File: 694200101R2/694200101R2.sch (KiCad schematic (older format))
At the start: 261 parts, among them J1 USB_C_Receptacle_USB2.0, J2 Conn_01x06_Male, J3 Conn_01x02_Male, SW1 MX_SW, SW10 MX_SW, SW100 MX_SW, SW101 MX_SW, SW102 MX_SW, SW103 MX_SW, SW104 MX_SW, SW105 MX_SW, SW106 MX_SW, SW107 MX_SW, SW11 MX_SW, SW12 MX_SW, SW13 MX_SW, SW14 MX_SW, SW15 MX_SW, SW16 MX_SW, SW17 MX_SW, SW18 MX_SW, SW19 MX_SW, SW2 MX_SW, SW20 MX_SW, SW21 MX_SW, SW22 MX_SW, SW23 MX_SW, SW24 MX_SW, SW25 MX_SW, SW26 MX_SW, SW27 MX_SW, SW28 MX_SW, SW29 MX_SW, SW3 MX_SW, SW30 MX_SW, SW31 MX_SW, SW32 MX_SW, SW33 MX_SW, SW34 MX_SW, SW35 MX_SW, SW36 MX_SW, SW37 MX_SW, SW38 MX_SW, SW39 MX_SW, SW4 MX_SW, SW40 MX_SW, SW41 MX_SW, SW42 MX_SW, SW43 MX_SW, SW44 MX_SW, SW45 MX_SW, SW46 MX_SW, SW47 MX_SW, SW48 MX_SW, SW49 MX_SW, SW5 MX_SW, SW50 MX_SW, SW51 MX_SW, SW52 MX_SW, SW53 MX_SW, SW54 MX_SW, SW55 MX_SW, SW56 MX_SW, SW57 MX_SW, SW58 MX_SW, SW59 MX_SW, SW6 MX_SW, SW60 MX_SW, SW61 MX_SW, SW62 MX_SW, SW63 MX_SW, SW64 MX_SW, SW65 MX_SW, SW66 MX_SW, SW67 MX_SW, SW68 MX_SW, SW69 MX_SW, SW7 MX_SW, SW70 MX_SW, SW71 MX_SW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

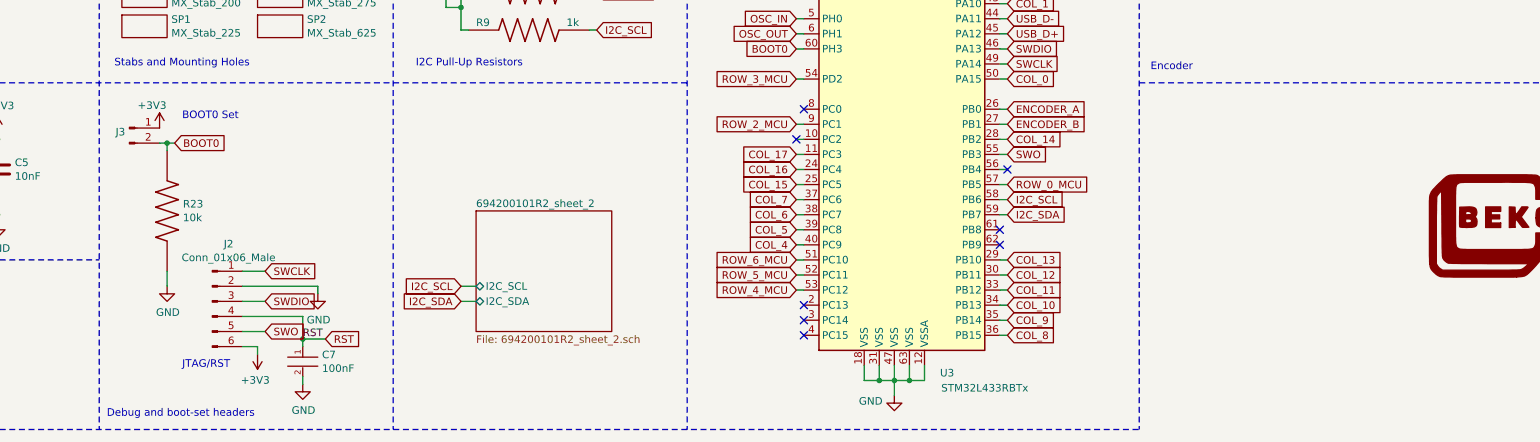
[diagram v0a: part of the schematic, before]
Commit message: Added BOOT0 Set and Reset Switches
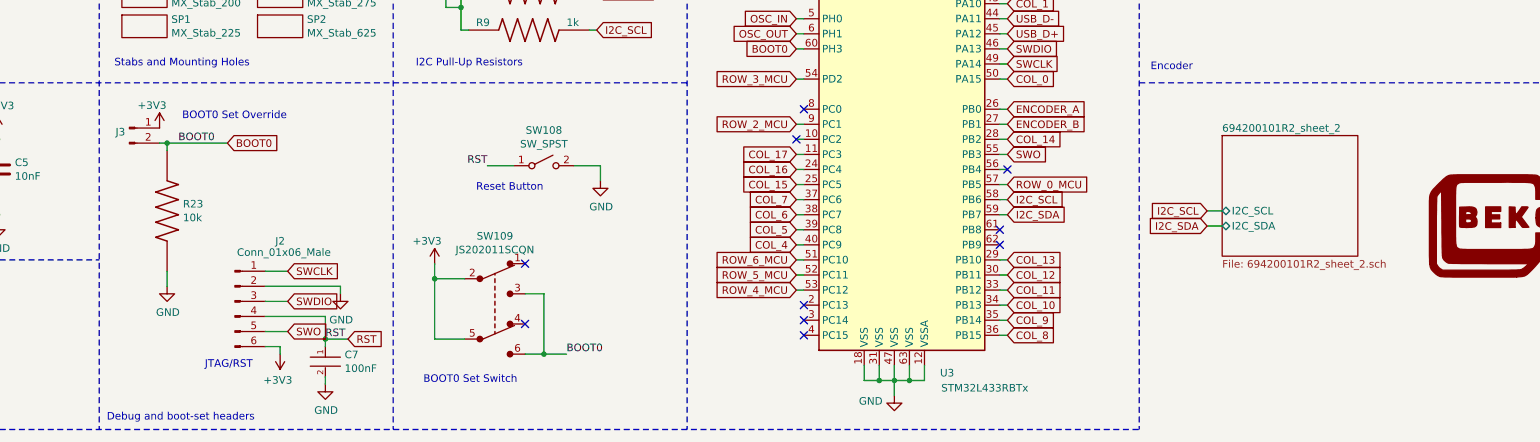
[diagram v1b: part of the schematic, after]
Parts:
- added SW108: SW_SPST, Button_Switch_SMD:SW_SPST_TL3342, symbol Switch:SW_SPST
- added SW109: JS202011SCQN, digikey-footprints:Switch_Slide_JS202011SCQN, symbol dk_Slide-Switches:JS202011SCQN
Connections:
- net +3V3: now also SW109.2, SW109.5
- net BOOT0: now also SW109.3, SW109.6
- net GND: now also SW108.2 (B)
- net RST: now also SW108.1 (A)
- no-connect marks 14 -> 16
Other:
- note added: "BOOT0 Set Override"
- note added: "BOOT0 Set Switch"
- note added: "Reset Button"
- note removed: "BOOT0 Set"
- moved on the sheet: C7, J2

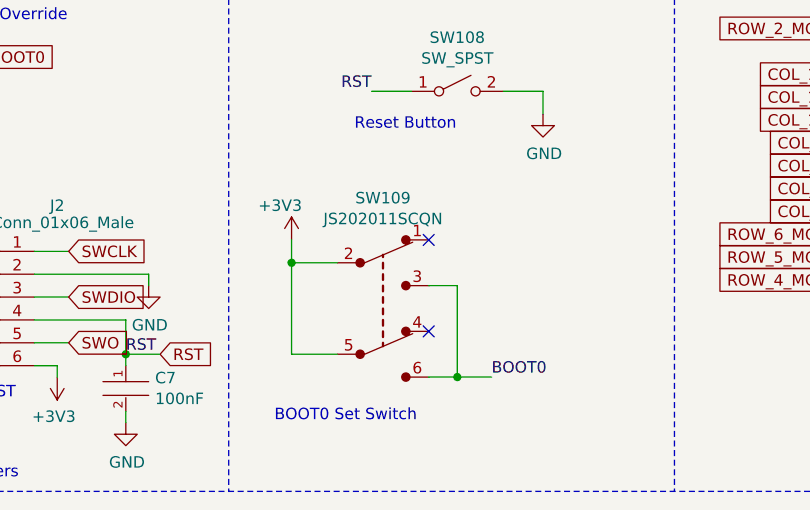
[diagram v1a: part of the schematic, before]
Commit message: Updated BOOT0 Switch to right angle switch
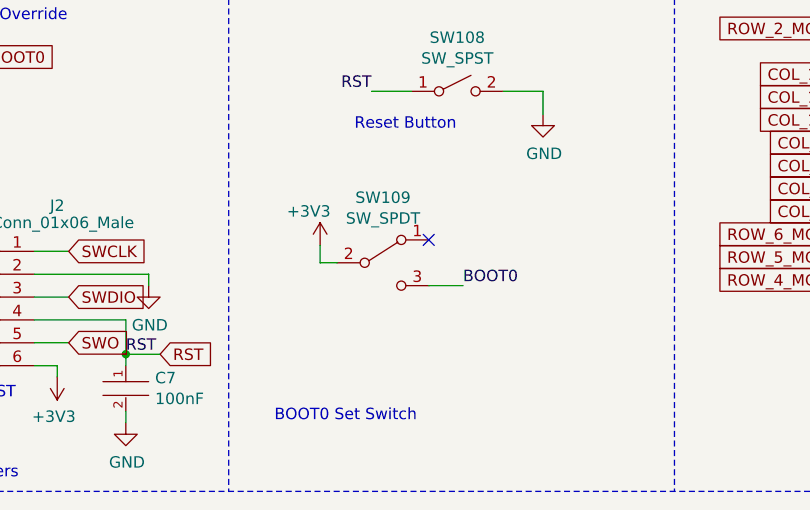
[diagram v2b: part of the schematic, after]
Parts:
- removed SW109: JS202011SCQN, digikey-footprints:Switch_Slide_JS202011SCQN, symbol dk_Slide-Switches:JS202011SCQN
- added SW109: SW_SPDT, Button_Switch_SMD:SW_SPDT_CK-JS102011SAQN, symbol Switch:SW_SPDT
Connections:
- net +3V3: now also SW109.2 (B)
- net BOOT0: now also SW109.3 (C)
- no-connect marks 16 -> 15
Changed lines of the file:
@@
 L power:+3V3 #PWR03
 U 1 1 630B8DFA
-P 6975 8600
-F 0 "#PWR03" H 6975 8450 50  0001 C CNN
-F 1 "+3V3" H 6925 8750 50  0000 C CNN
-F 2 "" H 6975 8600 50  0001 C CNN
-F 3 "" H 6975 8600 50  0001 C CNN
-	1    6975 8600
+P 7100 8625
+F 0 "#PWR03" H 7100 8475 50  0001 C CNN
+F 1 "+3V3" H 7050 8775 50  0000 C CNN
+F 2 "" H 7100 8625 50  0001 C CNN
+F 3 "" H 7100 8625 50  0001 C CNN
+	1    7100 8625
 	1    0    0    -1
 $EndComp
 Wire Wire Line
-	6975 8600 6975 8700
-Text Label 7850 9200 0    50   ~ 0
+	7100 8625 7100 8700
+Text Label 7725 8800 0    50   ~ 0
 BOOT0
-$Comp
-L dk_Slide-Switches:JS202011SCQN SW109
-U 1 1 63405795
-P 7375 8900
-F 0 "SW109" H 7375 9383 50  0000 C CNN
-F 1 "JS202011SCQN" H 7375 9292 50  0000 C CNN
-F 2 "digikey-footprints:Switch_Slide_JS202011SCQN" H 7575 9100 50  0001 L CNN
-F 3 "https://www.ckswitches.com/media/1422/js.pdf" H 7575 9200 60  0001 L CNN
-F 4 "401-2002-1-ND" H 7575 9300 60  0001 L CNN "Digi-Key_PN"
-F 5 "JS202011SCQN" H 7575 9400 60  0001 L CNN "MPN"
-F 6 "Switches" H 7575 9500 60  0001 L CNN "Category"
-F 7 "Slide Switches" H 7575 9600 60  0001 L CNN "Family"
-F 8 "https://www.ckswitches.com/media/1422/js.pdf" H 7575 9700 60  0001 L CNN "DK_Datasheet_Link"
-F 9 "/product-detail/en/c-k/JS202011SCQN/401-2002-1-ND/1640098" H 7575 9800 60  0001 L CNN "DK_Detail_Page"
-F 10 "SWITCH SLIDE DPDT 300MA 6V" H 7575 9900 60  0001 L CNN "Description"
-F 11 "C&K" H 7575 10000 60  0001 L CNN "Manufacturer"
-F 12 "Active" H 7575 10100 60  0001 L CNN "Status"
-	1    7375 8900
-	1    0    0    -1
-$EndComp
 Wire Wire Line
-	6975 8700 7175 8700
-Wire Wire Line
-	6975 8700 6975 9100
-Wire Wire Line
-	6975 9100 7175 9100
-Connection ~ 6975 8700
-NoConn ~ 7575 8600
-NoConn ~ 7575 9000
-Wire Wire Line
-	7575 8800 7700 8800
-Wire Wire Line
-	7700 8800 7700 9200
-Wire Wire Line
-	7700 9200 7575 9200
-Wire Wire Line
-	7700 9200 7850 9200
-Connection ~ 7700 9200
+	7100 8700 7175 8700
 Text Notes 6900 9400 0    50   ~ 0
 BOOT0 Set Switch
@@
 Text Notes 7250 8125 0    50   ~ 0
 Reset Button
+$Comp
+L Switch:SW_SPDT SW109
+U 1 1 62B1A803
+P 7375 8700
+F 0 "SW109" H 7375 8985 50  0000 C CNN
+F 1 "SW_SPDT" H 7375 8894 50  0000 C CNN
+F 2 "Button_Switch_SMD:SW_SPDT_CK-JS102011SAQN" H 7375 8700 50  0001 C CNN
+F 3 "~" H 7375 8700 50  0001 C CNN
+	1    7375 8700
+	1    0    0    -1
+$EndComp
+NoConn ~ 7575 8600
+Wire Wire Line
+	7575 8800 7725 8800
 $EndSCHEMATC

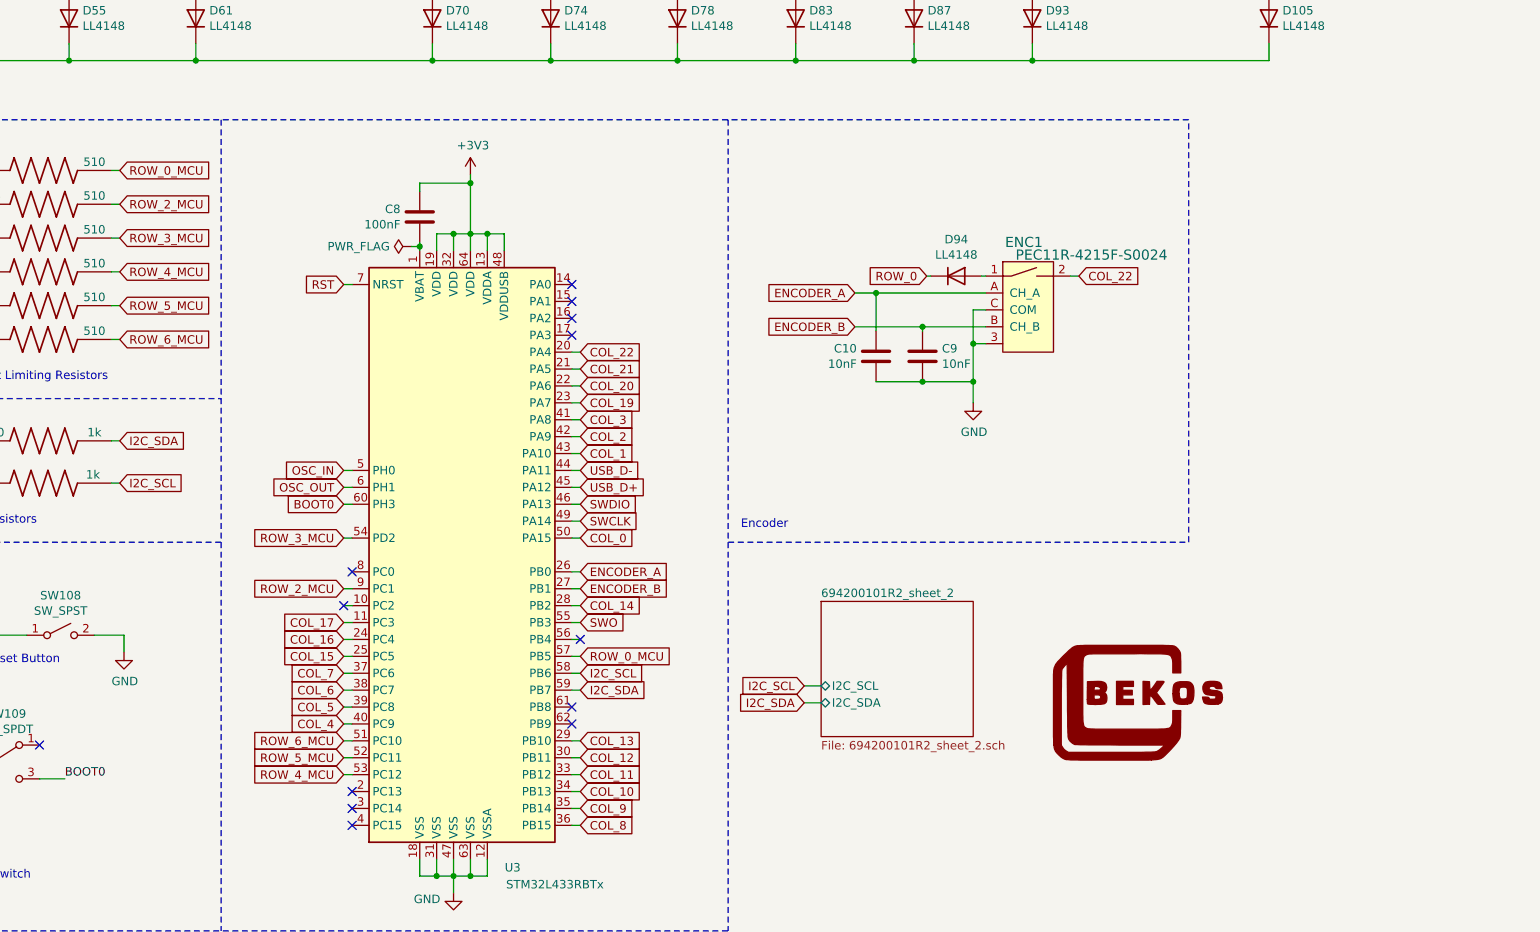
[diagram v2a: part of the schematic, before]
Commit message: Updated Schematic to use KiCad LED Driver Symbols
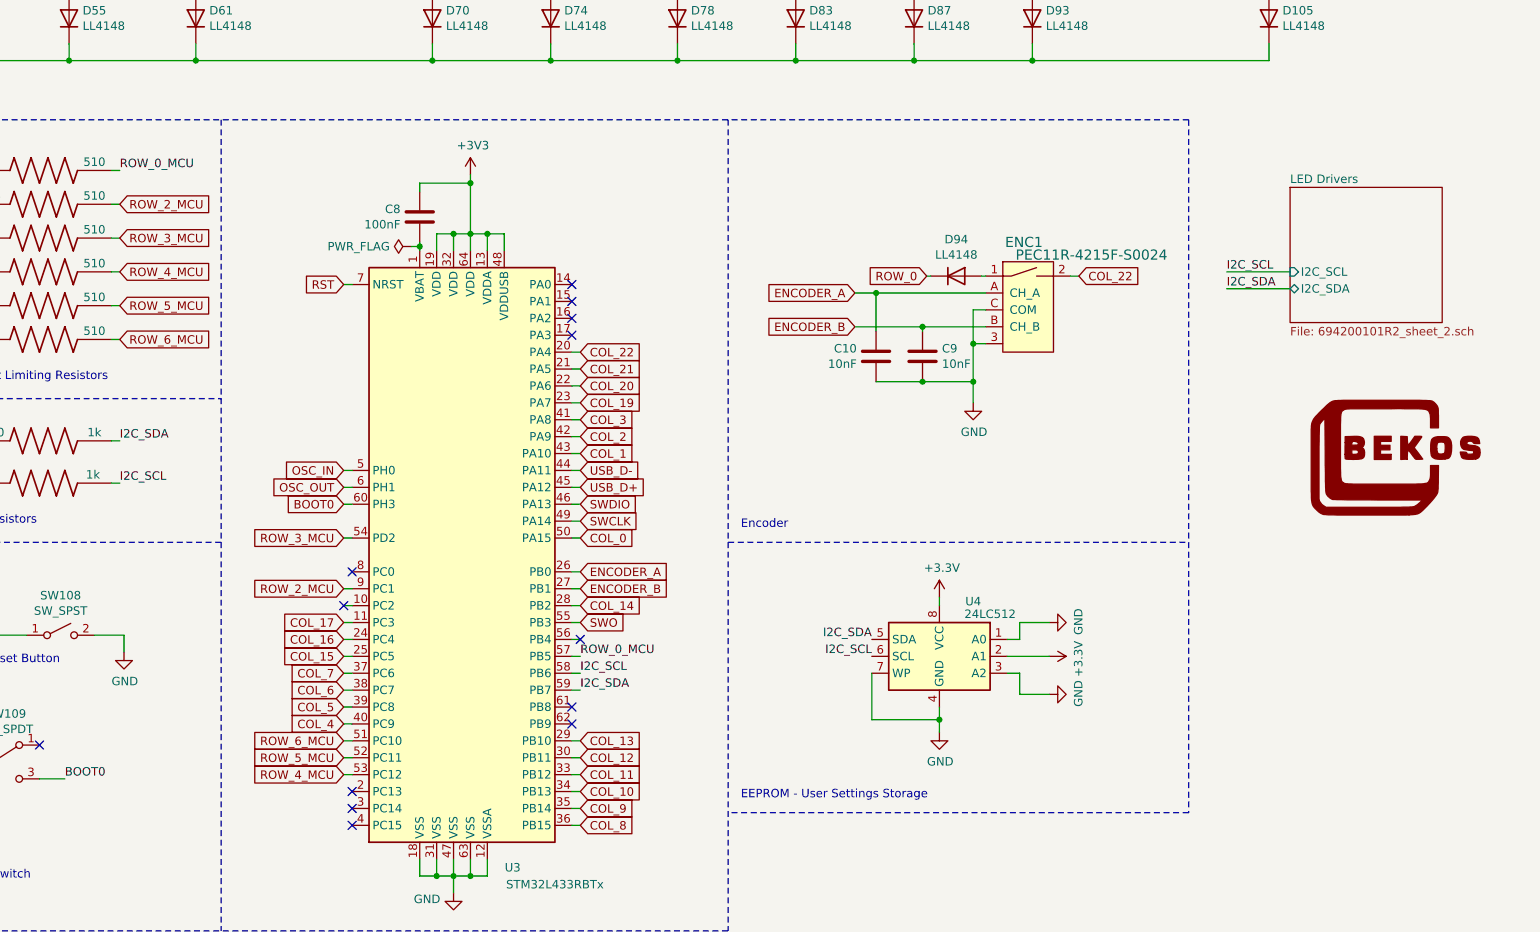
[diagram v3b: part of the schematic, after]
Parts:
- added U4: 24LC512, Package_SO:SO-8_3.9x4.9mm_P1.27mm, symbol Memory_EEPROM:24LC512
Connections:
- net +3V3: now also U4.2 (A1), U4.8 (VCC)
- net GND: now also U4.1 (A0), U4.3 (A2), U4.4 (GND), U4.7 (WP)
- net I2C_SCL: now also U4.6 (SCL)
- net I2C_SDA: now also U4.5 (SDA)
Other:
- note added: "EEPROM - User Settings Storage"
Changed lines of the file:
@@
 	5400 850  5400 1550
 Wire Wire Line
-	12200 8250 12100 8250
+	14975 5800 14600 5800
 Wire Wire Line
-	12200 8350 12100 8350
-Text GLabel 12100 8250 0    50   Input ~ 0
-I2C_SCL
-Text GLabel 12100 8350 0    50   Input ~ 0
-I2C_SDA
+	14975 5900 14600 5900
 Wire Wire Line
 	6100 900  6100 1550
@@
 Text GLabel 4350 6200 2    50   Input ~ 0
 USB_D+
-$Comp
-L BekosLogo:LOGO #G1
-U 1 1 6385997F
-P 14075 8350
-F 0 "#G1" H 14075 8040 60  0001 C CNN
-F 1 "LOGO" H 14075 8660 60  0001 C CNN
-F 2 "BekosLogo:BekosLogo" H 14075 8350 50  0001 C CNN
-F 3 "" H 14075 8350 50  0001 C CNN
-	1    14075 8350
-	1    0    0    -1
-$EndComp
 NoConn ~ 1750 6550
 NoConn ~ 1750 6450
@@
 Text GLabel 10775 7075 2    50   Input ~ 0
 USB_D+
-Text GLabel 10775 8275 2    50   Input ~ 0
-I2C_SDA
-Text GLabel 10775 8175 2    50   Input ~ 0
-I2C_SCL
 Wire Wire Line
 	10025 9375 10025 9475
@@
 Text GLabel 9375 8775 0    50   Input ~ 0
 ROW_4_MCU
-Text GLabel 8050 5200 2    50   Input ~ 0
-ROW_0_MCU
-Text GLabel 10775 8075 2    50   Input ~ 0
-ROW_0_MCU
 Wire Wire Line
 	8000 5400 8050 5400
@@
 Wire Wire Line
 	7200 5400 7150 5400
-Text GLabel 8050 7050 2    50   Input ~ 0
-I2C_SCL
-Text GLabel 8050 6800 2    50   Input ~ 0
-I2C_SDA
 Wire Wire Line
 	8050 7050 8000 7050
@@
 	11650 7400 14375 7400
 Wire Notes Line
-	14375 7400 14375 4900
-Wire Notes Line
 	650  4900 14375 4900
 Wire Notes Line
@@
 Wire Wire Line
 	3250 6875 3550 6875
-$Sheet
-S 12200 7750 900  800
-U 63A35802
-F0 "694200101R2_sheet_2" 50
-F1 "694200101R2_sheet_2.sch" 50
-F2 "I2C_SDA" B L 12200 8350 50
-F3 "I2C_SCL" B L 12200 8250 50
-$EndSheet
 $Comp
 L power:GND #PWR01
@@
 Wire Wire Line
 	7575 8800 7725 8800
+Text Label 10775 8175 0    50   ~ 0
+I2C_SCL
+Text Label 14600 5900 0    50   ~ 0
+I2C_SDA
+Text Label 10775 8275 0    50   ~ 0
+I2C_SDA
+Text Label 14600 5800 0    50   ~ 0
+I2C_SCL
+Text Label 8050 5200 0    50   ~ 0
+ROW_0_MCU
+Text Label 10775 8075 0    50   ~ 0
+ROW_0_MCU
+Text Label 8050 7050 0    50   ~ 0
+I2C_SCL
+Text Label 8050 6800 0    50   ~ 0
+I2C_SDA
+$Sheet
+S 14975 5300 900  800
+U 63A35802
+F0 "LED Drivers" 50
+F1 "694200101R2_sheet_2.sch" 50
+F2 "I2C_SDA" B L 14975 5900 50
+F3 "I2C_SCL" I L 14975 5800 50
+$EndSheet
+$Comp
+L BekosLogo:LOGO #G1
+U 1 1 6385997F
+P 15600 6900
+F 0 "#G1" H 15600 6590 60  0001 C CNN
+F 1 "LOGO" H 15600 7210 60  0001 C CNN
+F 2 "BekosLogo:BekosLogo" H 15600 6900 50  0001 C CNN
+F 3 "" H 15600 6900 50  0001 C CNN
+	1    15600 6900
+	1    0    0    -1
+$EndComp
+$Comp
+L power:GND #PWR?
+U 1 1 7325C2C0
+P 12900 8525
+AR Path="/63A35802/7325C2C0" Ref="#PWR?"  Part="1"
+AR Path="/7325C2C0" Ref="#PWR016"  Part="1"
+F 0 "#PWR016" H 12900 8275 50  0001 C CNN
+F 1 "GND" H 12905 8352 50  0000 C CNN
+F 2 "" H 12900 8525 50  0001 C CNN
+F 3 "" H 12900 8525 50  0001 C CNN
+	1    12900 8525
+	1    0    0    -1
+$EndComp
+Wire Wire Line
+	12500 8450 12900 8450
+Wire Wire Line
+	12900 8450 12900 8525
+Connection ~ 12900 8450
+$Comp
+L power:+3.3V #PWR?
+U 1 1 7325C2CA
+P 13550 8075
+AR Path="/63A35802/7325C2CA" Ref="#PWR?"  Part="1"
+AR Path="/7325C2CA" Ref="#PWR018"  Part="1"
+F 0 "#PWR018" H 13550 7925 50  0001 C CNN
+F 1 "+3.3V" H 13565 8248 50  0000 C CNN
+F 2 "" H 13550 8075 50  0001 C CNN
+F 3 "" H 13550 8075 50  0001 C CNN
+	1    13550 8075
+	0    1    1    0
+$EndComp
+Wire Wire Line
+	13375 7875 13550 7875
+Wire Wire Line
+	13375 7975 13375 7875
+Wire Wire Line
+	13375 8300 13550 8300
+Wire Wire Line
+	13375 8175 13375 8300
+$Comp
+L power:GND #PWR?
+U 1 1 7325C2D4
+P 13550 7875
+AR Path="/63A35802/7325C2D4" Ref="#PWR?"  Part="1"
+AR Path="/7325C2D4" Ref="#PWR017"  Part="1"
+F 0 "#PWR017" H 13550 7625 50  0001 C CNN
+F 1 "GND" H 13555 7702 50  0000 C CNN
+F 2 "" H 13550 7875 50  0001 C CNN
+F 3 "" H 13550 7875 50  0001 C CNN
+	1    13550 7875
+	0    -1   -1   0
+$EndComp
+$Comp
+L power:GND #PWR?
+U 1 1 7325C2DA
+P 13550 8300
+AR Path="/63A35802/7325C2DA" Ref="#PWR?"  Part="1"
+AR Path="/7325C2DA" Ref="#PWR019"  Part="1"
+F 0 "#PWR019" H 13550 8050 50  0001 C CNN
+F 1 "GND" H 13555 8127 50  0000 C CNN
+F 2 "" H 13550 8300 50  0001 C CNN
+F 3 "" H 13550 8300 50  0001 C CNN
+	1    13550 8300
+	0    -1   -1   0
+$EndComp
+$Comp
+L power:+3.3V #PWR?
+U 1 1 7325C2E0
+P 12900 7725
+AR Path="/63A35802/7325C2E0" Ref="#PWR?"  Part="1"
+AR Path="/7325C2E0" Ref="#PWR06"  Part="1"
+F 0 "#PWR06" H 12900 7575 50  0001 C CNN
+F 1 "+3.3V" H 12915 7898 50  0000 C CNN
+F 2 "" H 12900 7725 50  0001 C CNN
+F 3 "" H 12900 7725 50  0001 C CNN
+	1    12900 7725
+	1    0    0    -1
+$EndComp
+Wire Wire Line
+	12900 7725 12900 7775
+Wire Wire Line
+	12500 8175 12500 8450
+Wire Wire Line
+	12900 8375 12900 8450
+Wire Wire Line
+	13300 8175 13375 8175
+Wire Wire Line
+	13300 8075 13550 8075
+Wire Wire Line
+	13300 7975 13375 7975
+$Comp
+L Memory_EEPROM:24LC512 U?
+U 1 1 7325C2EC
+P 12900 8075
+AR Path="/63A35802/7325C2EC" Ref="U?"  Part="1"
+AR Path="/7325C2EC" Ref="U4"  Part="1"
+F 0 "U4" H 12700 8400 50  0000 C CNN
+F 1 "24LC512" H 12600 8325 50  0000 C CNN
+F 2 "Package_SO:SO-8_3.9x4.9mm_P1.27mm" H 12900 8075 50  0001 C CNN
+F 3 "http://ww1.microchip.com/downloads/en/DeviceDoc/21754M.pdf" H 12900 8075 50  0001 C CNN
+	1    12900 8075
+	-1   0    0    -1
+$EndComp
+Text Label 12500 8075 2    50   ~ 0
+I2C_SCL
+Text Label 12500 7975 2    50   ~ 0
+I2C_SDA
+Wire Notes Line
+	14375 9000 11650 9000
+Wire Notes Line
+	14375 4900 14375 9000
+Text Notes 11725 8925 0    50   ~ 0
+EEPROM - User Settings Storage
 $EndSCHEMATC
